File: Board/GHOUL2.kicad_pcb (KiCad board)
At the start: 2 copper layers, 105.4 x 88.9 mm, 21 parts

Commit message: work in progress...
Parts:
- 0.3 Ohm Res.: renamed from 0.3Ohm Res.
- LM1084 Adj.: renamed from Voltage Reg.
- moved G*** 8.89 mm to (132.1, 109.2)
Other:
- board text added: "Resources Available Online: bpp.umd.edu/wiki https://github.com/UMDBPP/GHOUL or email us at nearspace@ssl.umd.edu"
- board text removed: "Resources Available Online: bpp.umd.edu https://github.com/UMDBPP/GHOUL"
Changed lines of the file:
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@@
     (property "Sheetname" "")
     (attr smd)
-    (fp_text reference "MOSFET 2" (at -10.59 -1.67 270) (layer "F.SilkS")
+    (fp_text reference "MOSFET 2" (at -10.59 -0.019 270) (layer "F.SilkS")
       (effects (font (size 1 1) (thickness 0.15)))
     )
@@
   )
   (footprint "GHOULFootPrints:GHOULFootprint" (layer "F.Cu")
-    (at 123.19 109.22)
+    (at 132.08 109.22)
     (attr board_only exclude_from_pos_files exclude_from_bom)
     (fp_text reference "G***" (at -48.26 30.48) (layer "F.SilkS")
@@
     (property "Sheetname" "")
     (attr smd)
-    (fp_text reference "0.3Ohm Res." (at 9.84 0 270) (layer "F.SilkS")
+    (fp_text reference "0.3 Ohm Res." (at 9.84 0 270) (layer "F.SilkS")
       (effects (font (size 1 1) (thickness 0.15)))
     )
@@
     (property "Sheetname" "")
     (attr smd)
-    (fp_text reference "Voltage Reg." (at 9.84 0 90) (layer "F.SilkS")
+    (fp_text reference "LM1084 Adj." (at 9.84 0 90) (layer "F.SilkS")
       (effects (font (size 1 1) (thickness 0.15)))
     )
@@
       (effects (font (size 1 1) (thickness 0.15)) (justify mirror))
     )
-    (fp_line (start -7.56 13.21) (end 2.56 13.21) (layer "B.SilkS") (width 0.12))
-    (fp_line (start 2.56 13.21) (end 2.56 11.11) (layer "B.SilkS") (width 0.12))
-    (fp_line (start -7.56 13.21) (end -7.56 11.11) (layer "B.SilkS") (width 0.12))
-    (fp_line (start 2.56 8.89) (end 2.56 3.99) (layer "B.SilkS") (width 0.12))
-    (fp_line (start 2.56 8.89) (end 3.15 8.89) (layer "B.SilkS") (width 0.12))
-    (fp_line (start 2.56 11.11) (end 3.15 11.11) (layer "B.SilkS") (width 0.12))
-    (fp_line (start -8.15 8.89) (end -7.56 8.89) (layer "B.SilkS") (width 0.12))
-    (fp_line (start -7.56 3.99) (end 2.56 3.99) (layer "B.SilkS") (width 0.12))
-    (fp_line (start -8.15 11.11) (end -7.56 11.11) (layer "B.SilkS") (width 0.12))
-    (fp_line (start -7.56 8.89) (end -7.56 3.99) (layer "B.SilkS") (width 0.12))
-    (fp_arc (start -8.15 11.11) (mid -9.26 10) (end -8.15 8.89) (layer "B.SilkS") (width 0.12))
-    (fp_arc (start 3.15 8.89) (mid 4.26 10) (end 3.15 11.11) (layer "B.SilkS") (width 0.12))
     (fp_line (start -8.15 11) (end -7.45 11) (layer "B.Fab") (width 0.1))
     (fp_line (start -7.45 9) (end -7.45 4.1) (layer "B.Fab") (width 0.1))
@@
     (effects (font (size 1 1) (thickness 0.15)) (justify left mirror))
   )
-  (gr_text "Venting makes me feel good" (at 122.555 133.985) (layer "B.SilkS")
+  (gr_text "Venting makes me feel good" (at 134.62 133.985) (layer "B.SilkS")
     (effects (font (size 1 1) (thickness 0.15)) (justify mirror))
   )
-  (gr_text "Resources Available Online:\n\nbpp.umd.edu\n\nhttps://github.com/UMDBPP/GHOUL" (at 198.755 125.095) (layer "B.SilkS")
+  (gr_text "Resources Available Online:\n\nbpp.umd.edu/wiki\n\nhttps://github.com/UMDBPP/GHOUL\n\nor email us at nearspace@ssl.umd.edu" (at 198.755 125.095) (layer "B.SilkS")
     (effects (font (size 1 1) (thickness 0.15)) (justify left mirror))
   )
@@
     (polygon
       (pts
-        (xy 182.88 106.093847)
-        (xy 190.5 111.173847)
-        (xy 190.5 115.443)
-        (xy 172.72 115.443)
-        (xy 172.72 99.06)
-        (xy 182.88 99.06)
+        (xy 182.88 107.442)
+        (xy 190.5 108.712)
+        (xy 190.5 115.062)
+        (xy 181.61 115.062)
+        (xy 172.72 110.744)
+        (xy 172.72 98.298)
+        (xy 182.88 98.298)
       )
     )
@@
     (polygon
       (pts
-        (xy 197.993 115.824)
-        (xy 193.04 115.824)
+        (xy 197.993 115.062)
+        (xy 193.04 115.062)
         (xy 193.04 120.015)
         (xy 182.88 120.015)
         (xy 182.88 115.57)
         (xy 190.5 115.57)
-        (xy 190.5 102.997)
-        (xy 193.04 102.997)
-        (xy 198.12 102.997)
+        (xy 190.5 103.632)
+        (xy 193.04 103.632)
+        (xy 198.12 103.632)
       )
     )
@@
     (polygon
       (pts
-        (xy 198.12 102.743)
-        (xy 193.167 102.743)
+        (xy 198.12 101.981)
+        (xy 193.167 101.981)
         (xy 190.5 99.06)
         (xy 187.96 96.52)
-        (xy 187.96 86.36)
-        (xy 198.12 86.36)
+        (xy 187.96 85.598)
+        (xy 198.12 85.598)
       )
     )
@@
     (polygon
       (pts
-        (xy 198.12 134.62)
-        (xy 187.96 134.62)
+        (xy 198.12 134.874)
+        (xy 187.96 134.874)
         (xy 187.96 121.92)
         (xy 187.96 119.38)
-        (xy 193.04 115.824)
-        (xy 198.12 115.824)
+        (xy 193.04 116.586)
+        (xy 198.12 116.586)
       )
     )

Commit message: cleaned up some things
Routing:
- net GND: track 129.5 -> 84.6 mm, vias 28 -> 32
- net Vin: track 91.1 -> 122.9 mm, vias 8 -> 7
- net SCL: track 54.0 -> 36.6 mm
- net SDA: track 59.0 -> 46.3 mm
- net 3v3 pwr: track 26.9 -> 25.8 mm, vias 0 -> 1
- net 5v pwr: track 171.1 -> 171.9 mm
- net Xbee DOut: track 25.1 -> 25.8 mm
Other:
- board text added: "PWM-PWR-GND-Feedback Servo"
- board text added: "Version 2.0 HAB Helium Venting Board Produced by: Michael Kalin, Kruti Bhingradiya, Jeremy Kuznetsov, Daniel Grammer, and Akemi Takeuchi Maryland Space Grant Consortium Balloon Payload Program Space Systems Lab Univ. of Maryland, College Park (2023)"
- board text removed: "PWM-PWR-GND-Feedback"
- board text removed: "Version 2.0 HAB Helium Venting Board Produced by: Michael Kalin, Kruti Bhingradiya, Jeremy Kuznetsov, Daniel Grammer, and Akemi Takeuchi Univ. of Maryland, College Park (2023)"

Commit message: i think we are pretty close to being done
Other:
- board text added: "PWM-PWR-GND-Feedback"
- board text removed: "PWM-PWR-GND-Feedback Servo"
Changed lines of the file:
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@@
     (effects (font (size 1 1) (thickness 0.15)) (justify left mirror))
   )
-  (gr_text "PWM-PWR-GND-Feedback\nServo" (at 112.395 77.47) (layer "F.SilkS")
+  (gr_text "PWM-PWR-GND-Feedback" (at 112.395 77.47) (layer "F.SilkS")
     (effects (font (size 1 1) (thickness 0.15)))
   )

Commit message: for real this time... ?
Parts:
- J1: renamed from Power Input
- Q1: renamed from MOSFET 2
- Q2: renamed from MOSFET 1
- R1: renamed from 0.3 Ohm Res.
- U1: renamed from Teensy 3.5
- U4: renamed from Feedback Servo
- U5: renamed from LM1084 Adj.
- U6: renamed from Cut-Down 1
- U7: renamed from GPS Breakout
- U8: renamed from Xbee Breakout
- U9: renamed from Cut-Down 2
- renumbered Capacitor to C1, Accelerometer to U10, LM7805 to U2, BMP280 to U3
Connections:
- U7 pad 10: (no net) -> unconnected-(U1-Pad8)
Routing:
- net unconnected-(U1-Pad8): track 0.00 -> 45.4 mm
- net unconnected-(U1-Pad7): track 0.00 -> 36.0 mm
- net Net-(BT1-Pad1): track 41.5 -> 18.5 mm
- net Net-(U1-Pad12): track 42.4 -> 50.1 mm
- net Net-(U1-Pad11): track 48.4 -> 56.1 mm
- net 5v pwr: track 171.9 -> 170.0 mm
- net SDA: track 46.3 -> 47.7 mm
- net SCL: track 36.6 -> 37.4 mm

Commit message: done for now, not because its necesarily done but because im tired
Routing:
- net unconnected-(U1-Pad8): track 45.4 -> 42.5 mm
- net 5v pwr: track 170.0 -> 172.1 mm
- net unconnected-(U1-Pad7): track 36.0 -> 35.0 mm
- net Net-(U1-Pad12): track 50.1 -> 49.1 mm
- net Net-(U1-Pad11): track 56.1 -> 55.0 mm

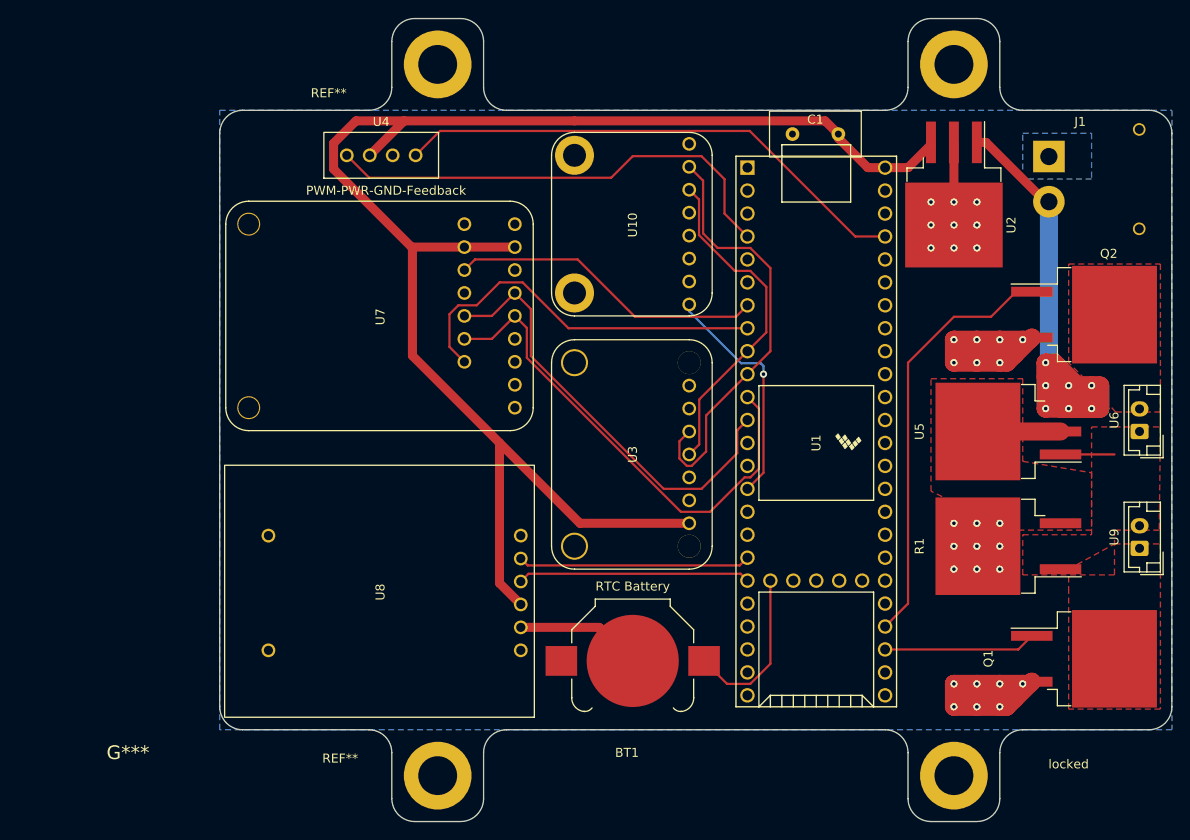
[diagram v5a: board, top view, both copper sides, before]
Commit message: Finished up fixed kalins silly error deleting all my cool labels
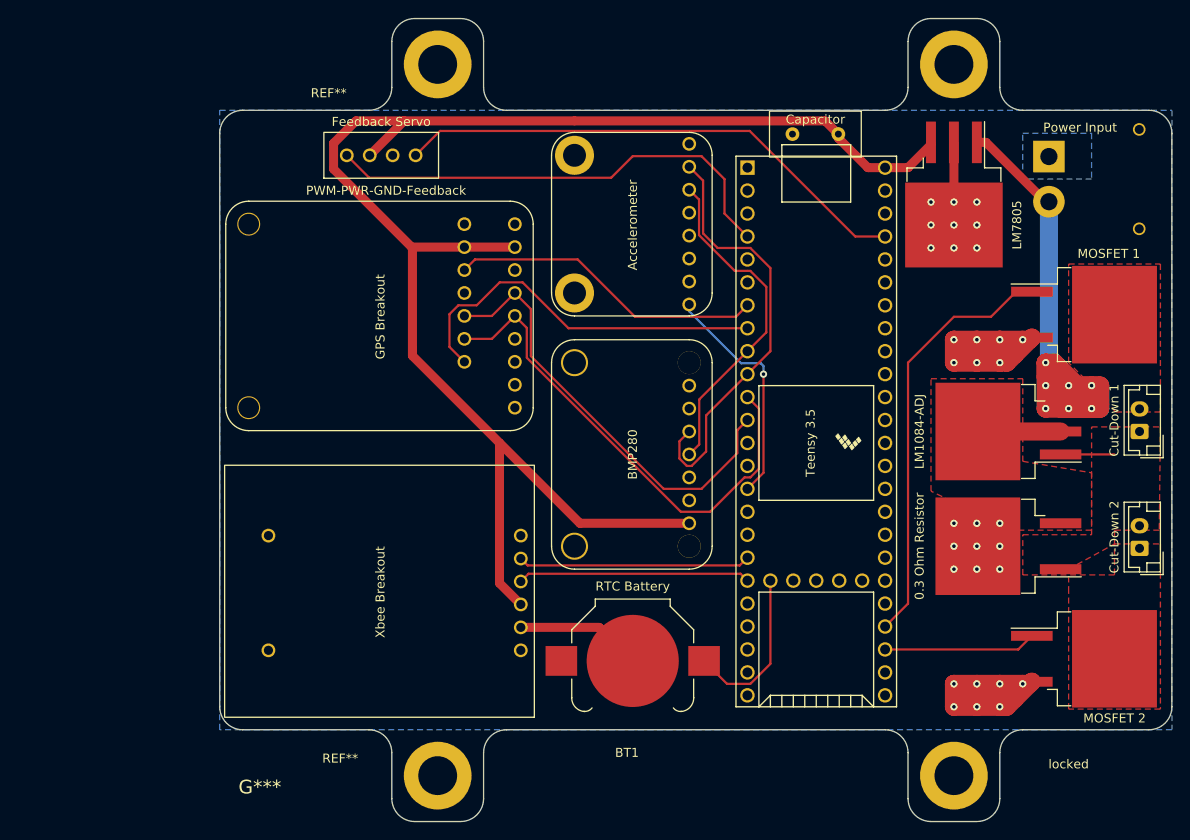
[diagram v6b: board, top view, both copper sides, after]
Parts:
- 0.3 Ohm Resistor: renamed from R1
- Cut-Down 1: renamed from U6
- Cut-Down 2: renamed from U9
- Feedback Servo: renamed from U4
- GPS Breakout: renamed from U7
- MOSFET 1: renamed from Q2
- MOSFET 2: renamed from Q1
- Power Input: renamed from J1
- Teensy 3.5: renamed from U1
- Xbee Breakout: renamed from U8
- renumbered U10 to Accelerometer, U3 to BMP280, C1 to Capacitor, U5 to LM1084-ADJ, U2 to LM7805
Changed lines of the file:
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@@
     (property "Sheetname" "")
     (attr through_hole)
-    (fp_text reference "U10" (at 10.065 -8.795 90 unlocked) (layer "F.SilkS")
+    (fp_text reference "Accelerometer" (at 10.065 -8.795 90 unlocked) (layer "F.SilkS")
       (effects (font (size 1 1) (thickness 0.15)))
     )
@@
     (property "Sheetname" "")
     (attr through_hole)
-    (fp_text reference "U1" (at 1.27 0 90) (layer "F.SilkS")
+    (fp_text reference "Teensy 3.5" (at 1.27 0.635 90) (layer "F.SilkS")
       (effects (font (size 1 1) (thickness 0.15)))
     )
@@
     (property "Sheetname" "")
     (attr smd)
-    (fp_text reference "Q1" (at -10.59 -0.019 270) (layer "F.SilkS")
+    (fp_text reference "MOSFET 2" (at 3.38 6.585) (layer "F.SilkS")
       (effects (font (size 1 1) (thickness 0.15)))
     )
@@
     (property "Sheetname" "")
     (attr through_hole)
-    (fp_text reference "U3" (at 0 -8.795 90 unlocked) (layer "F.SilkS")
+    (fp_text reference "BMP280" (at 0 -8.795 90 unlocked) (layer "F.SilkS")
       (effects (font (size 1 1) (thickness 0.15)))
     )
@@
     (property "Sheetname" "")
     (attr through_hole)
-    (fp_text reference "C1" (at 5.08 -0.921 unlocked) (layer "F.SilkS")
+    (fp_text reference "Capacitor" (at 5.08 -0.921 unlocked) (layer "F.SilkS")
       (effects (font (size 1 1) (thickness 0.15)))
     )
@@
     (property "Sheetname" "")
     (attr smd)
-    (fp_text reference "U2" (at 3.375 -6.35 90) (layer "F.SilkS")
+    (fp_text reference "LM7805" (at 3.375 -6.985 90) (layer "F.SilkS")
       (effects (font (size 1 1) (thickness 0.15)))
     )
@@
     (property "Sheetname" "")
     (attr through_hole)
-    (fp_text reference "U4" (at 6.35 -6.255 unlocked) (layer "F.SilkS")
+    (fp_text reference "Feedback Servo" (at 6.35 -6.255 unlocked) (layer "F.SilkS")
       (effects (font (size 1 1) (thickness 0.15)))
     )
@@
     (at 132.08 109.22)
     (attr board_only exclude_from_pos_files exclude_from_bom)
-    (fp_text reference "G***" (at -48.26 30.48) (layer "F.SilkS")
+    (fp_text reference "G***" (at -33.655 34.29) (layer "F.SilkS")
       (effects (font (size 1.524 1.524) (thickness 0.3)))
     )
@@
     (property "Sheetname" "")
     (attr through_hole)
-    (fp_text reference "U6" (at 1.25 -2.8 90) (layer "F.SilkS")
+    (fp_text reference "Cut-Down 1" (at 1.25 -2.8 90) (layer "F.SilkS")
       (effects (font (size 1 1) (thickness 0.15)))
     )
@@
     (property "Sheetname" "")
     (attr through_hole)
-    (fp_text reference "U8" (at 13.855 -17.05 90 unlocked) (layer "F.SilkS")
+    (fp_text reference "Xbee Breakout" (at 13.855 -17.05 90 unlocked) (layer "F.SilkS")
       (effects (font (size 1 1) (thickness 0.15)))
     )
@@
     (property "Sheetname" "")
     (attr through_hole)
-    (fp_text reference "U7" (at 12.605 -16.923 90 unlocked) (layer "F.SilkS")
+    (fp_text reference "GPS Breakout" (at 12.605 -16.923 90 unlocked) (layer "F.SilkS")
       (effects (font (size 1 1) (thickness 0.15)))
     )
@@
     (property "Sheetname" "")
     (attr smd)
-    (fp_text reference "R1" (at 9.84 0 270) (layer "F.SilkS")
+    (fp_text reference "0.3 Ohm Resistor" (at 9.84 0 270) (layer "F.SilkS")
       (effects (font (size 1 1) (thickness 0.15)))
     )
@@
     (property "Sheetname" "")
     (attr smd)
-    (fp_text reference "Q2" (at 2.74 -6.75 180) (layer "F.SilkS")
+    (fp_text reference "MOSFET 1" (at 2.74 -6.75 180) (layer "F.SilkS")
       (effects (font (size 1 1) (thickness 0.15)))
     )
@@
     (property "Sheetname" "")
     (attr smd)
-    (fp_text reference "U5" (at 9.84 0 90) (layer "F.SilkS")
+    (fp_text reference "LM1084-ADJ" (at 9.84 0 90) (layer "F.SilkS")
       (effects (font (size 1 1) (thickness 0.15)))
     )
@@
     (property "Sheetname" "")
     (attr through_hole)
-    (fp_text reference "U9" (at 1.25 -2.8 90) (layer "F.SilkS")
+    (fp_text reference "Cut-Down 2" (at 1.25 -2.8 90) (layer "F.SilkS")
       (effects (font (size 1 1) (thickness 0.15)))
     )
@@
     (property "Sheetname" "")
     (attr through_hole)
-    (fp_text reference "J1" (at 3.85 3.455) (layer "F.SilkS")
+    (fp_text reference "Power Input" (at 3.215 3.455) (layer "F.SilkS")
       (effects (font (size 1 1) (thickness 0.15)))
     )

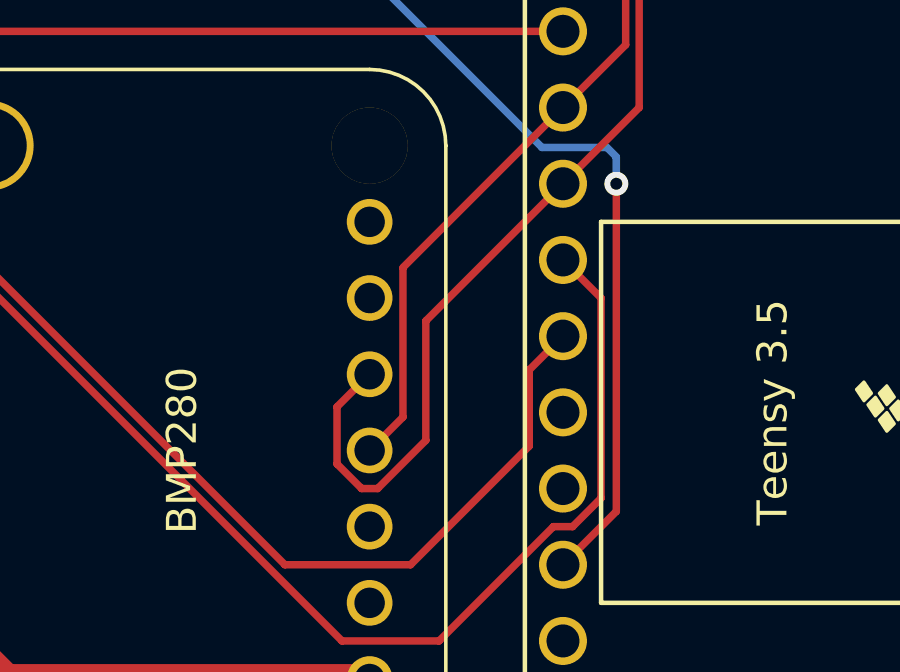
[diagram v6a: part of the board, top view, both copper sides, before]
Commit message: fixed schematic and brd bmp280 miswiring
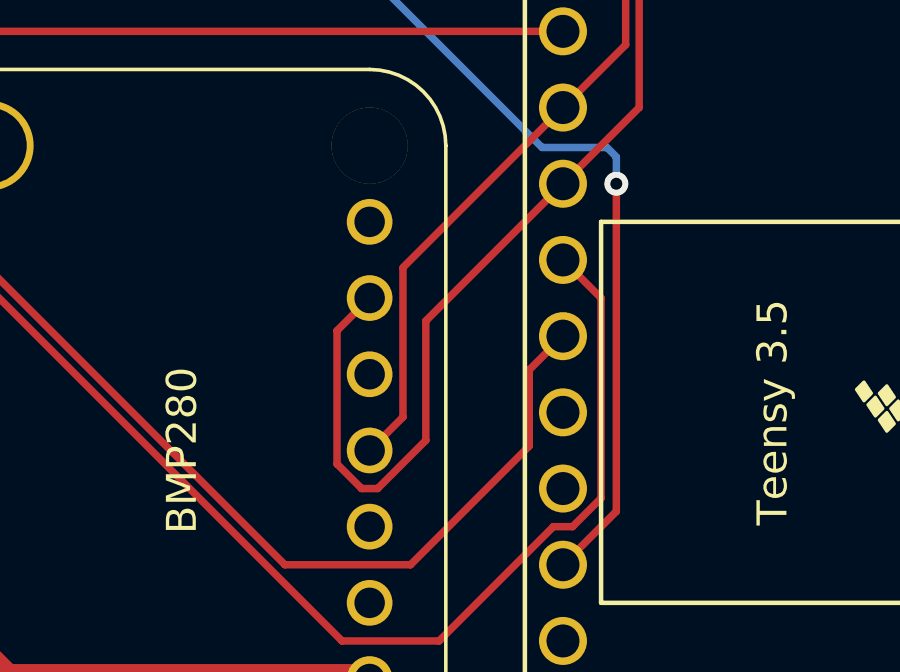
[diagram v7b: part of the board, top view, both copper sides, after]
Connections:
- BMP280 pad 5: SDA -> (no net)
- BMP280 pad 6: unconnected-(U3-Pad6) -> SDA
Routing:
- net SDA: track 47.7 -> 50.2 mm
